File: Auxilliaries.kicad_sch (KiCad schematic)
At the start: 5 parts, among them J4 FAN, J5 FAN, U2 LM317

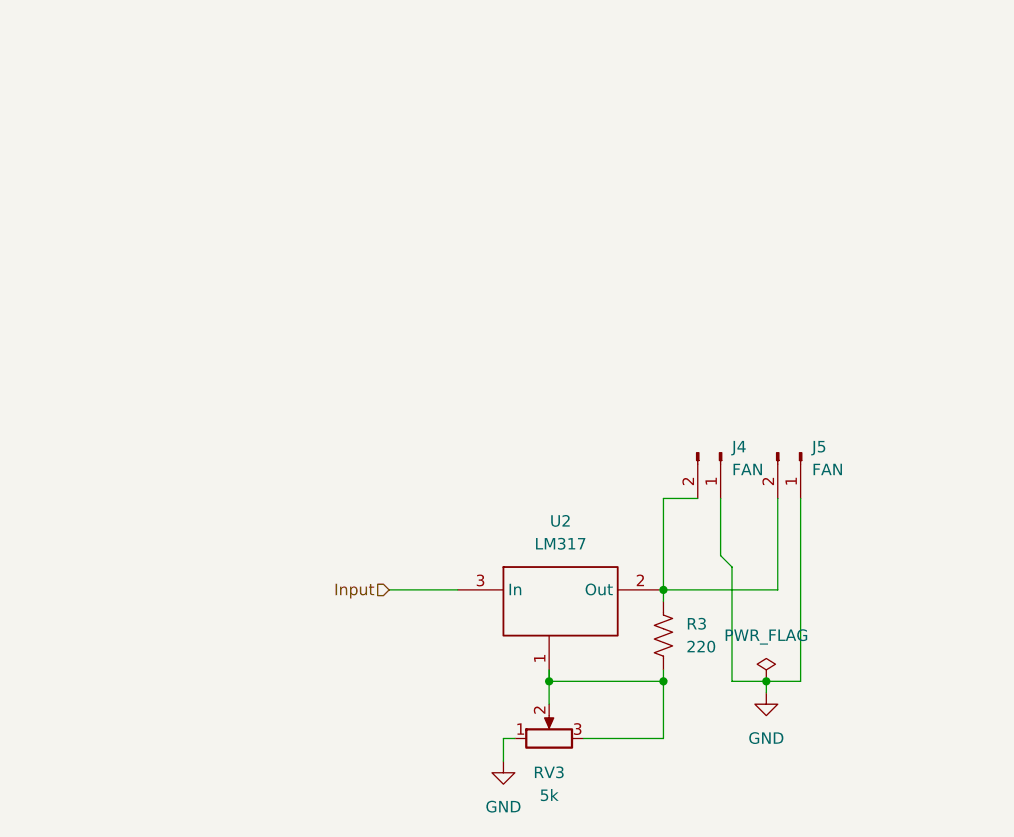
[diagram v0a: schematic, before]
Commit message: Updates to the schematic to make use of the centre tapped transformer to get negative rail.
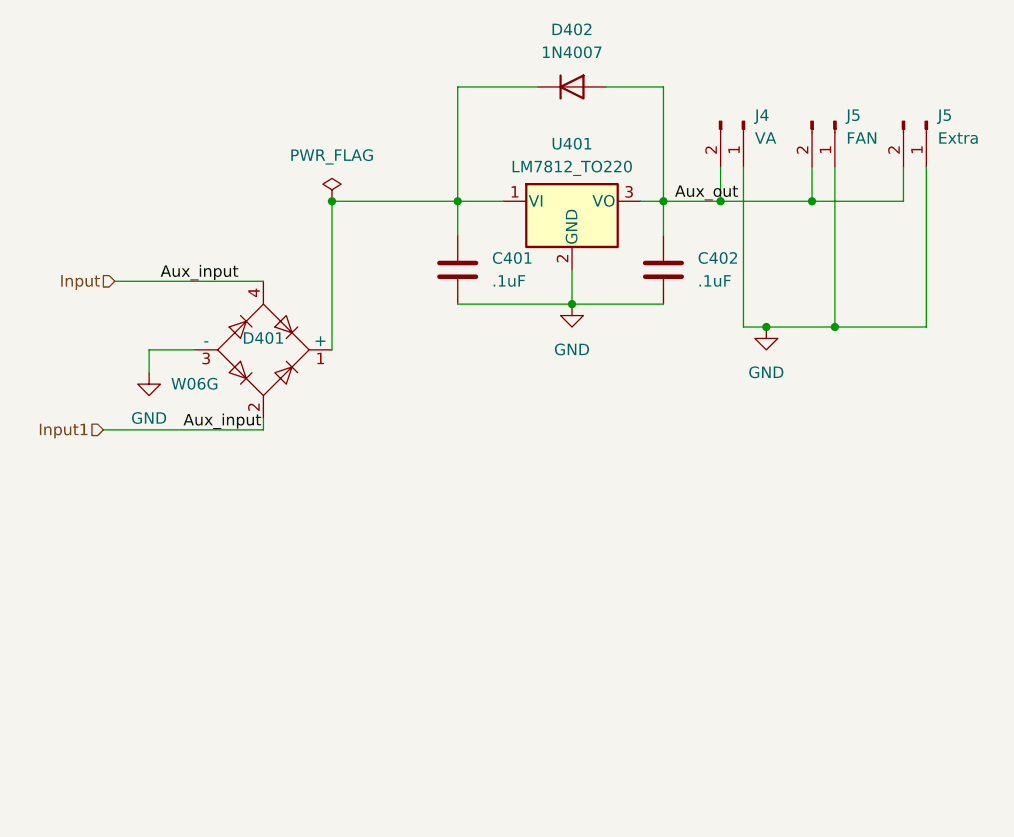
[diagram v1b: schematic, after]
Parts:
- removed J5: FAN, Connector_PinHeader_2.54mm:PinHeader_1x02_P2.54mm_Vertical, symbol Connector:Conn_01x02_Pin
- removed R3: 220, Resistor_THT:R_Axial_DIN0207_L6.3mm_D2.5mm_P10.16mm_Horizontal, symbol Device:R_US
- removed RV3: 5k, Potentiometer_THT:Potentiometer_Bourns_3296W_Vertical, symbol Device:R_Potentiometer
- removed U2: LM317, Package_TO_SOT_THT:TO-126-3_Vertical, symbol V_Regulator:LM317
- added C401, C402: .1uF, Capacitor_THT:C_Disc_D4.3mm_W1.9mm_P5.00mm, symbol Device:C
- added D401: W06G, Diode_THT:Diode_Bridge_Round_D9.8mm, symbol Diode_Bridge:W06G
- added D402: 1N4007, Diode_THT:D_DO-41_SOD81_P10.16mm_Horizontal, symbol Diode:1N4007
- added J5: FAN, Connector_PinHeader_2.54mm:PinHeader_1x02_P2.54mm_Vertical, symbol Connector:Conn_01x02_Pin
- added J5: Extra, Connector_PinHeader_2.54mm:PinHeader_1x02_P2.54mm_Vertical, symbol Connector:Conn_01x02_Pin
- added U401: LM7812_TO220, Package_TO_SOT_THT:TO-220-3_Vertical, symbol Regulator_Linear:LM7812_TO220
- J4: value FAN -> VA
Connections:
- net GND: now also C401.2, C402.2, D401.3 (-), J5.1 (Pin_1), J5.1 (Pin_1), U401.2 (GND)
- net Input: now also D401.2, D401.4
- net Aux_out: now reaches J4.2 (Pin_2)
- net Aux_out: now also C402.1, D402.2 (A), J5.2 (Pin_2), J5.2 (Pin_2), U401.3 (VO)
- new net: C401.1, D401.1 (+), D402.1 (K), U401.1 (VI)
